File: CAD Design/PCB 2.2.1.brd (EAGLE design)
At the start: 70 x 44.9 mm, 46 parts, among them U1 CC2538, U2 MAX1555, X1 32MHz, X2 FC-12M

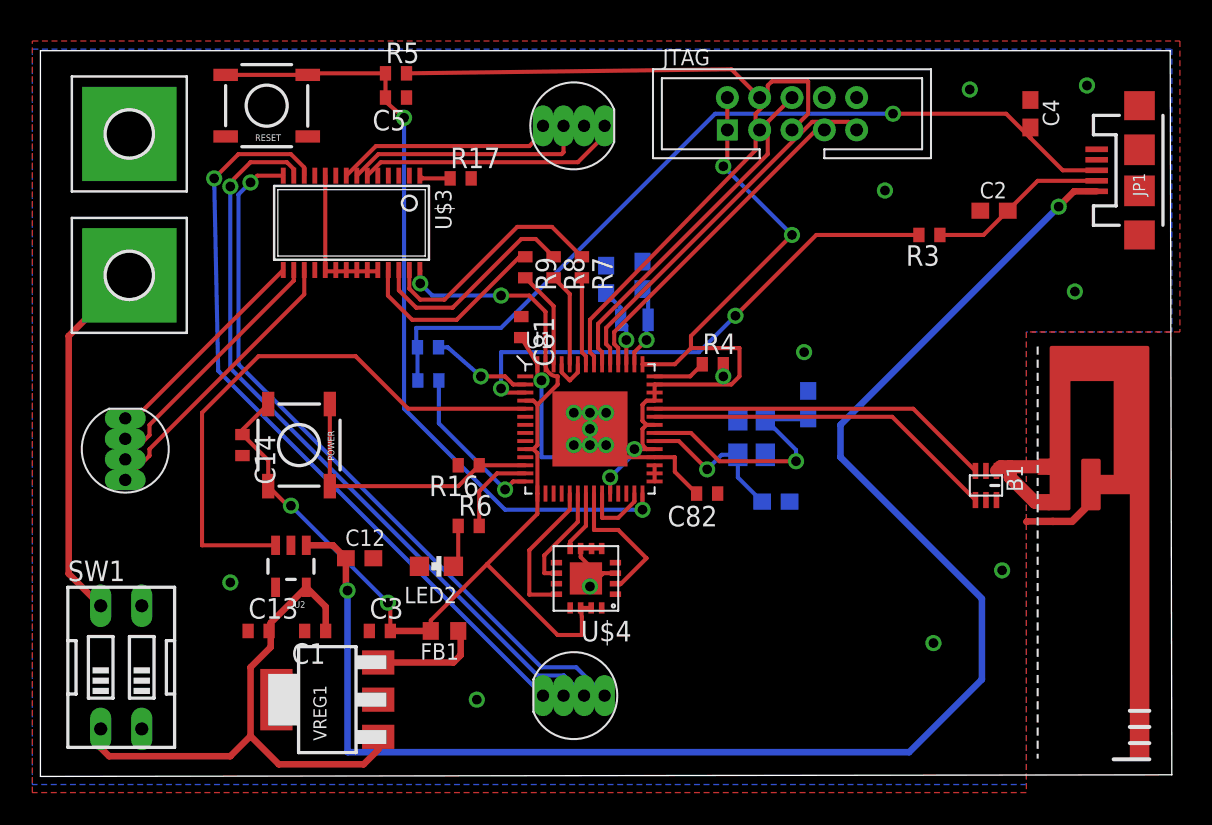
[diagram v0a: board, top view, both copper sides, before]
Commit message: Correction
Correcting 2.2.1 with most current save
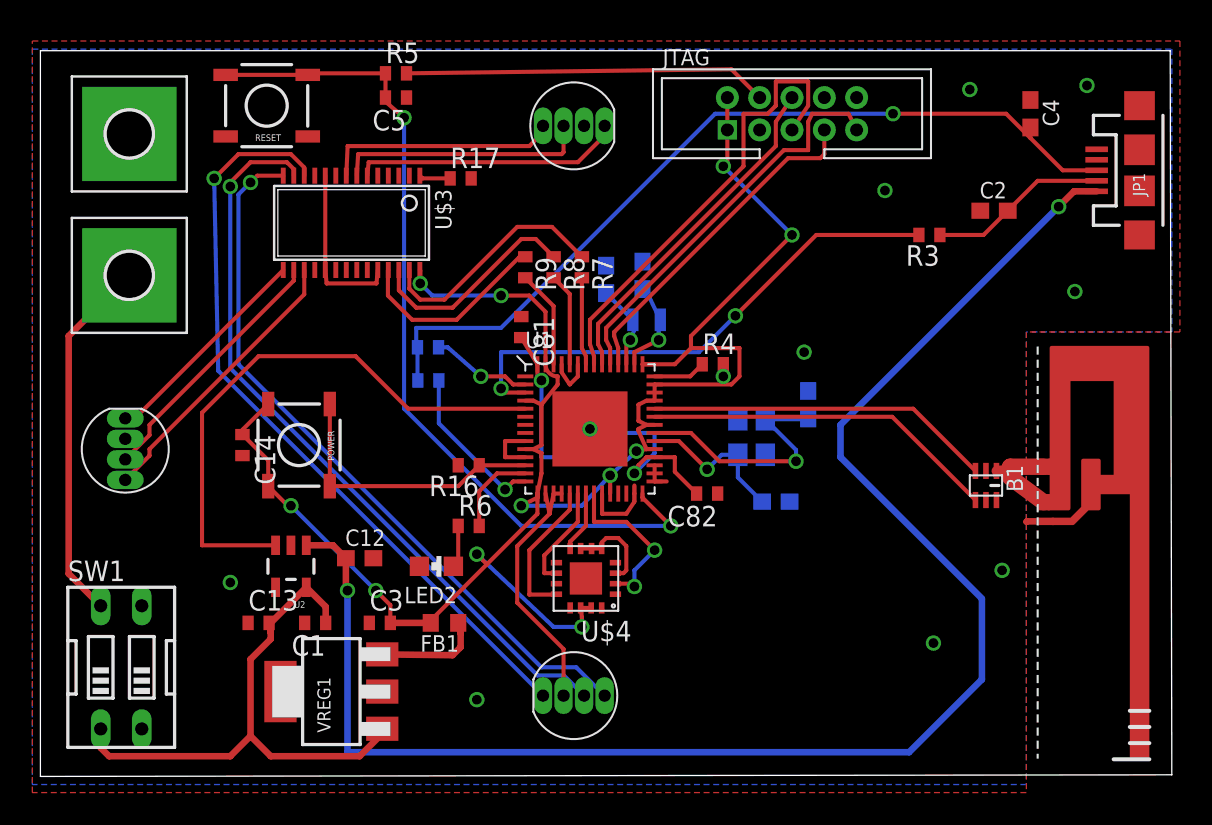
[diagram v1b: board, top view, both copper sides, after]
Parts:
- moved X2 0.75 mm to (37.5, 28.2)
- moved VREG1 0.56 mm to (18.0, 5.25)
- moved C1 0.50 mm to (17.0, 9.50)
- moved C13 0.50 mm to (13.5, 9.50)
- moved C3 0.50 mm to (21.0, 9.50)
- moved FB1 0.50 mm to (25.0, 9.50)
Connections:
- removed net GND3: U$4.3, U$4.5, U$4.6, U$4.7
- removed net N$32: U$3.10, U$3.19, U$3.24
- net GND: now also U$3.10, U$3.19, U$3.24, U$4.3, U$4.5, U$4.6, U$4.7
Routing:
- net GND: track 10.0 -> 47.6 mm
- net N$32: track 9.15 -> 0.00 mm
- net 3V3: track 109.7 -> 118.3 mm, vias 8 -> 11
- net GND3: track 5.94 -> 0.00 mm, vias 1 -> 0
- net DCOUPL: track 19.5 -> 24.2 mm
- net !RST_PIN: track 49.7 -> 53.6 mm
- net N$6: track 23.3 -> 25.0 mm
- net N$16: track 8.80 -> 10.2 mm, vias 0 -> 2
- net N$18: track 13.7 -> 14.7 mm
- net N$7: track 20.3 -> 21.1 mm
- net N$40: track 5.15 -> 5.90 mm
- net N$15: track 15.0 -> 15.7 mm
- net PB6: track 27.9 -> 28.5 mm
